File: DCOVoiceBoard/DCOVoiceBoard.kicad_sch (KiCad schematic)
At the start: 0 parts

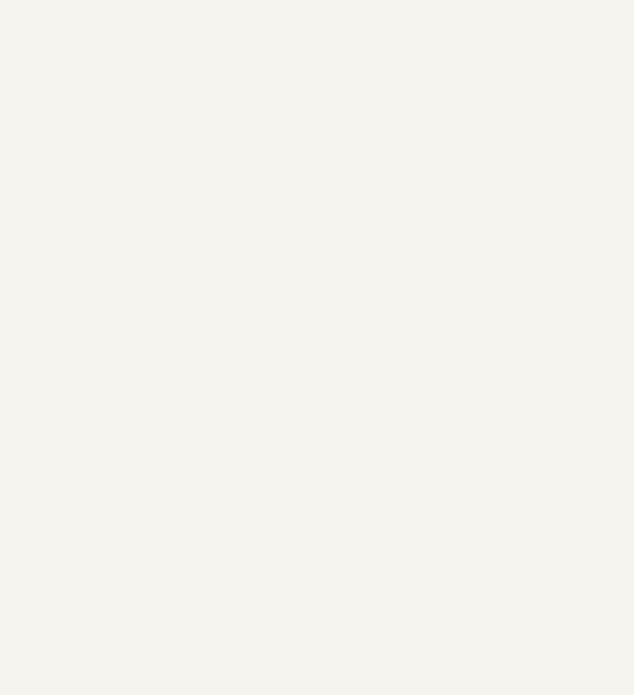
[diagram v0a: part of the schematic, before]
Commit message: voice board rough schematic
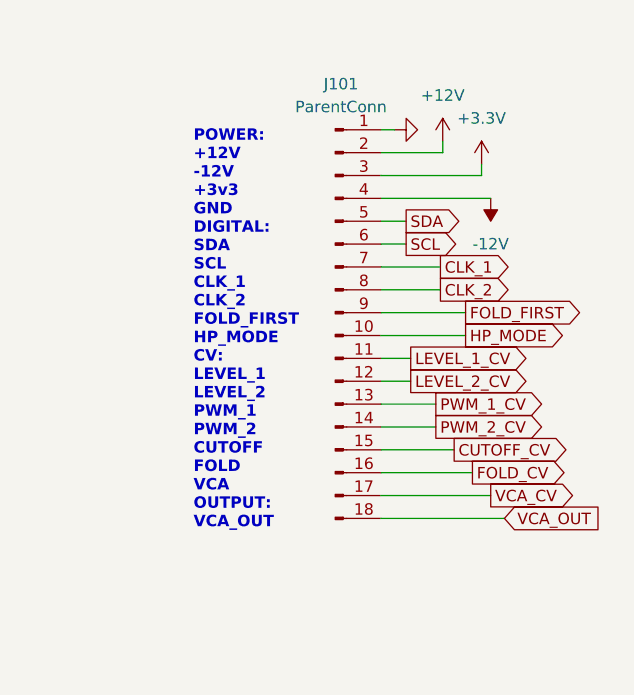
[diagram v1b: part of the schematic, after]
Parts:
- added J101: ParentConn, symbol Connector:Conn_01x18_Pin
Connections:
- new net +12V: J101.2 (Pin_2)
- new net +3.3V: J101.3 (Pin_3)
- new net -12V: J101.4 (Pin_4)
- new net CLK_1: J101.7 (Pin_7)
- new net CLK_2: J101.8 (Pin_8)
- new net CUTOFF_CV: J101.15 (Pin_15)
- new net FOLD_CV: J101.16 (Pin_16)
- new net FOLD_FIRST: J101.9 (Pin_9)
- new net GND: J101.1 (Pin_1)
- new net HP_MODE: J101.10 (Pin_10)
- new net LEVEL_1_CV: J101.11 (Pin_11)
- new net LEVEL_2_CV: J101.12 (Pin_12)
- new net PWM_1_CV: J101.13 (Pin_13)
- new net PWM_2_CV: J101.14 (Pin_14)
- new net SCL: J101.6 (Pin_6)
- new net SDA: J101.5 (Pin_5)
- new net VCA_CV: J101.17 (Pin_17)
- new net VCA_OUT: J101.18 (Pin_18)
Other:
- note added: "POWER: +12V -12V +3v3 GND DIGITAL: SDA SCL CLK_1 CLK_2 FOLD_FIRST HP_MODE CV: LEVEL_1 LEVEL_2 PWM_1 PWM_2 CUTOFF FOLD VCA OUTPUT: VCA_OUT"

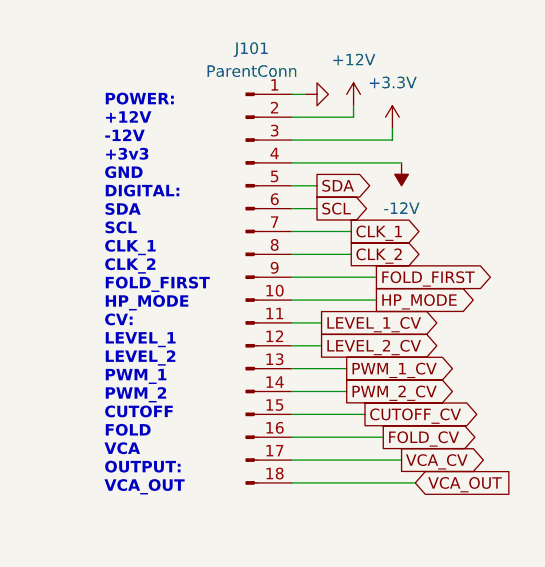
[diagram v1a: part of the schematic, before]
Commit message: net classes, osc layout
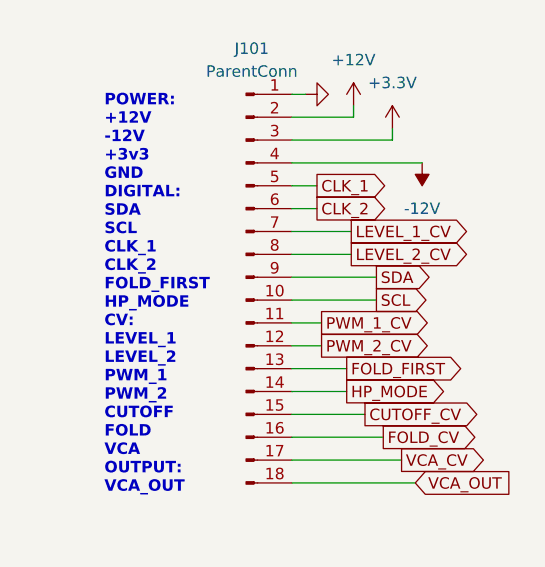
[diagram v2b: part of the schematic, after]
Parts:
- J101: footprint (none) -> Connector_PinHeader_2.54mm:PinHeader_1x18_P2.54mm_Vertical
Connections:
- net CLK_1: now also J101.5 (Pin_5); no longer J101.7 (Pin_7)
- net CLK_2: now also J101.6 (Pin_6); no longer J101.8 (Pin_8)
- net FOLD_FIRST: now also J101.13 (Pin_13); no longer J101.9 (Pin_9)
- net HP_MODE: now also J101.14 (Pin_14); no longer J101.10 (Pin_10)
- net LEVEL_1_CV: now also J101.7 (Pin_7); no longer J101.11 (Pin_11)
- net LEVEL_2_CV: now also J101.8 (Pin_8); no longer J101.12 (Pin_12)
- net PWM_1_CV: now also J101.11 (Pin_11); no longer J101.13 (Pin_13)
- net PWM_2_CV: now also J101.12 (Pin_12); no longer J101.14 (Pin_14)
- net SCL: now also J101.10 (Pin_10); no longer J101.6 (Pin_6)
- net SDA: now also J101.9 (Pin_9); no longer J101.5 (Pin_5)
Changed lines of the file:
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@@
     (stroke (width 0) (type default))
   )
-  (wire (pts (xy 119.888 43.18) (xy 132.08 43.18))
+  (wire (pts (xy 119.888 43.18) (xy 134.366 43.18))
     (stroke (width 0) (type default))
   )
@@
     (effects (font (size 1.27 1.27) bold) (justify left bottom))
   )
-  (global_label "PWM_2_CV" (shape output) (at 125.984 68.58 0) (fields_autoplaced)
-    (effects (font (size 1.27 1.27)) (justify left))
-    (property "Intersheetrefs" "${INTERSHEET_REFS}" (at 138.6453 68.58 0)
+  (global_label "PWM_2_CV" (shape output) (at 123.19 63.5 0) (fields_autoplaced)
+    (effects (font (size 1.27 1.27)) (justify left))
+    (property "Intersheetrefs" "${INTERSHEET_REFS}" (at 135.8513 63.5 0)
       (effects (font (size 1.27 1.27)) (justify left) hide)
     )
@@
     )
   )
-  (global_label "CLK_1" (shape output) (at 126.492 50.8 0) (fields_autoplaced)
-    (effects (font (size 1.27 1.27)) (justify left))
-    (property "Intersheetrefs" "${INTERSHEET_REFS}" (at 135.2224 50.8 0)
-      (effects (font (size 1.27 1.27)) (justify left) hide)
-    )
-  )
-  (global_label "SCL" (shape output) (at 122.682 48.26 0) (fields_autoplaced)
-    (effects (font (size 1.27 1.27)) (justify left))
-    (property "Intersheetrefs" "${INTERSHEET_REFS}" (at 129.1748 48.26 0)
-      (effects (font (size 1.27 1.27)) (justify left) hide)
-    )
-  )
-  (global_label "PWM_1_CV" (shape output) (at 125.984 66.04 0) (fields_autoplaced)
-    (effects (font (size 1.27 1.27)) (justify left))
-    (property "Intersheetrefs" "${INTERSHEET_REFS}" (at 138.6453 66.04 0)
+  (global_label "CLK_1" (shape output) (at 122.682 45.72 0) (fields_autoplaced)
+    (effects (font (size 1.27 1.27)) (justify left))
+    (property "Intersheetrefs" "${INTERSHEET_REFS}" (at 131.4124 45.72 0)
+      (effects (font (size 1.27 1.27)) (justify left) hide)
+    )
+  )
+  (global_label "SCL" (shape output) (at 129.286 58.42 0) (fields_autoplaced)
+    (effects (font (size 1.27 1.27)) (justify left))
+    (property "Intersheetrefs" "${INTERSHEET_REFS}" (at 135.7788 58.42 0)
+      (effects (font (size 1.27 1.27)) (justify left) hide)
+    )
+  )
+  (global_label "PWM_1_CV" (shape output) (at 123.19 60.96 0) (fields_autoplaced)
+    (effects (font (size 1.27 1.27)) (justify left))
+    (property "Intersheetrefs" "${INTERSHEET_REFS}" (at 135.8513 60.96 0)
       (effects (font (size 1.27 1.27)) (justify left) hide)
     )
@@
     )
   )
-  (global_label "LEVEL_2_CV" (shape output) (at 123.19 63.5 0) (fields_autoplaced)
-    (effects (font (size 1.27 1.27)) (justify left))
-    (property "Intersheetrefs" "${INTERSHEET_REFS}" (at 137.1213 63.5 0)
+  (global_label "LEVEL_2_CV" (shape output) (at 126.492 53.34 0) (fields_autoplaced)
+    (effects (font (size 1.27 1.27)) (justify left))
+    (property "Intersheetrefs" "${INTERSHEET_REFS}" (at 140.4233 53.34 0)
       (effects (font (size 1.27 1.27)) (justify left) hide)
     )
@@
     )
   )
-  (global_label "CLK_2" (shape output) (at 126.492 53.34 0) (fields_autoplaced)
-    (effects (font (size 1.27 1.27)) (justify left))
-    (property "Intersheetrefs" "${INTERSHEET_REFS}" (at 135.2224 53.34 0)
-      (effects (font (size 1.27 1.27)) (justify left) hide)
-    )
-  )
-  (global_label "SDA" (shape output) (at 122.682 45.72 0) (fields_autoplaced)
-    (effects (font (size 1.27 1.27)) (justify left))
-    (property "Intersheetrefs" "${INTERSHEET_REFS}" (at 129.2353 45.72 0)
-      (effects (font (size 1.27 1.27)) (justify left) hide)
-    )
-  )
-  (global_label "HP_MODE" (shape output) (at 129.286 58.42 0) (fields_autoplaced)
-    (effects (font (size 1.27 1.27)) (justify left))
-    (property "Intersheetrefs" "${INTERSHEET_REFS}" (at 141.0402 58.42 0)
-      (effects (font (size 1.27 1.27)) (justify left) hide)
-    )
-  )
-  (global_label "FOLD_FIRST" (shape output) (at 129.286 55.88 0) (fields_autoplaced)
-    (effects (font (size 1.27 1.27)) (justify left))
-    (property "Intersheetrefs" "${INTERSHEET_REFS}" (at 143.0965 55.88 0)
-      (effects (font (size 1.27 1.27)) (justify left) hide)
-    )
-  )
-  (global_label "LEVEL_1_CV" (shape output) (at 123.19 60.96 0) (fields_autoplaced)
-    (effects (font (size 1.27 1.27)) (justify left))
-    (property "Intersheetrefs" "${INTERSHEET_REFS}" (at 137.1213 60.96 0)
+  (global_label "CLK_2" (shape output) (at 122.682 48.26 0) (fields_autoplaced)
+    (effects (font (size 1.27 1.27)) (justify left))
+    (property "Intersheetrefs" "${INTERSHEET_REFS}" (at 131.4124 48.26 0)
+      (effects (font (size 1.27 1.27)) (justify left) hide)
+    )
+  )
+  (global_label "SDA" (shape output) (at 129.286 55.88 0) (fields_autoplaced)
+    (effects (font (size 1.27 1.27)) (justify left))
+    (property "Intersheetrefs" "${INTERSHEET_REFS}" (at 135.8393 55.88 0)
+      (effects (font (size 1.27 1.27)) (justify left) hide)
+    )
+  )
+  (global_label "HP_MODE" (shape output) (at 125.984 68.58 0) (fields_autoplaced)
+    (effects (font (size 1.27 1.27)) (justify left))
+    (property "Intersheetrefs" "${INTERSHEET_REFS}" (at 137.7382 68.58 0)
+      (effects (font (size 1.27 1.27)) (justify left) hide)
+    )
+  )
+  (global_label "FOLD_FIRST" (shape output) (at 125.984 66.04 0) (fields_autoplaced)
+    (effects (font (size 1.27 1.27)) (justify left))
+    (property "Intersheetrefs" "${INTERSHEET_REFS}" (at 139.7945 66.04 0)
+      (effects (font (size 1.27 1.27)) (justify left) hide)
+    )
+  )
+  (global_label "LEVEL_1_CV" (shape output) (at 126.492 50.8 0) (fields_autoplaced)
+    (effects (font (size 1.27 1.27)) (justify left))
+    (property "Intersheetrefs" "${INTERSHEET_REFS}" (at 140.4233 50.8 0)
       (effects (font (size 1.27 1.27)) (justify left) hide)
     )
@@
       (effects (font (size 1.27 1.27)))
     )
-    (property "Footprint" "" (at 114.808 55.88 0)
+    (property "Footprint" "Connector_PinHeader_2.54mm:PinHeader_1x18_P2.54mm_Vertical" (at 114.808 55.88 0)
       (effects (font (size 1.27 1.27)) hide)
     )
@@
     )
   )
-  (symbol (lib_id "power:-12V") (at 132.08 43.18 180) (unit 1)
-    (in_bom yes) (on_board yes) (dnp no) (fields_autoplaced)
-    (property "Reference" "#PWR0104" (at 132.08 45.72 0)
-      (effects (font (size 1.27 1.27)) hide)
-    )
-    (property "Value" "-12V" (at 132.08 48.26 0)
-      (effects (font (size 1.27 1.27)))
-    )
-    (property "Footprint" "" (at 132.08 43.18 0)
-      (effects (font (size 1.27 1.27)) hide)
-    )
-    (property "Datasheet" "" (at 132.08 43.18 0)
-      (effects (font (size 1.27 1.27)) hide)
-    )
+  (symbol (lib_id "power:-12V") (at 134.366 43.18 180) (unit 1)
+    (in_bom yes) (on_board yes) (dnp no) (fields_autoplaced)
+    (property "Reference" "#PWR0104" (at 134.366 45.72 0)
+      (effects (font (size 1.27 1.27)) hide)
+    )
+    (property "Value" "-12V" (at 134.366 48.26 0)
+      (effects (font (size 1.27 1.27)))
+    )
+    (property "Footprint" "" (at 134.366 43.18 0)
+      (effects (font (size 1.27 1.27)) hide)
+    )
+    (property "Datasheet" "" (at 134.366 43.18 0)
+      (effects (font (size 1.27 1.27)) hide)
+    )

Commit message: motherboard hardware
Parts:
- removed J101: ParentConn, Connector_PinHeader_2.54mm:PinHeader_1x18_P2.54mm_Vertical, symbol Connector:Conn_01x18_Pin
- added C302 (x2), C303 (x2): 100n, Capacitor_SMD:C_0805_2012Metric, symbol Device:C
- added J101: VoiceHeader, Connector_PinHeader_2.54mm:PinHeader_1x18_P2.54mm_Vertical, symbol Connector:VoiceBoardConnector_18p
- added U302 (x2): TMUX4053, Package_SO:TSSOP-16_4.4x5mm_P0.65mm, symbol Analog_Switch:TMUX4053
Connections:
- net +12V: now also C302.1, C302.1, J101.2 (+12V), U302.16 (VDD), U302.16 (VDD)
- net +3.3V: now also J101.3 (+3v3)
- net -12V: now also C303.1, C303.1, J101.4 (-12V), U302.7 (VSS), U302.7 (VSS)
- net CLK_1: now also J101.6 (CLK1)
- net CLK_2: now also J101.5 (CLK2)
- net CUTOFF_CV: now also J101.13 (CutoffCV)
- net FOLD_CV: now also J101.14 (FoldCV)
- net FOLD_FIRST: now also J101.11 (FoldFirst), U302.10 (S2), U302.11 (S1), U302.9 (S3), U302.9 (S3)
- net GND: now also C302.2, C302.2, C303.2, C303.2, J101.1 (GND), U302.2 (B0), U302.6 (INH), U302.6 (INH), U302.8 (GND), U302.8 (GND)
- net HP_MODE: now also J101.12 (HPMode), U302.10 (S2), U302.11 (S1)
- net LEVEL_1_CV: now also J101.8 (L1)
- net LEVEL_2_CV: now also J101.7 (L2)
- net PWM_1_CV: now also J101.10 (PWM1)
- net PWM_2_CV: now also J101.9 (PWM2)
- net SCL: now also J101.18 (SCL)
- net SDA: now also J101.17 (SDA)
- net VCA_CV: now also J101.15 (VCACV)
- net VCA_OUT: now also J101.16 (VoiceOut)
- new net FILTER_IN: U302.1 (B1), U302.12 (A0), U302.13 (A1), U302.4 (C)
- new net FILTER_OUT: U302.2 (B0), U302.4 (C)
- new net FOLDER_IN: U302.15 (B), U302.5 (C0)
- new net FOLDER_OUT: U302.14 (A), U302.3 (C1)
- new net HP_IN: U302.15 (B)
- new net LP_IN: U302.14 (A)
- new net OSC_MIX: U302.1 (B1), U302.5 (C0)
- new net VCA_IN: U302.12 (A0), U302.3 (C1)
- no-connect marks 0 -> 1
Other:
- note added: "Logic high on 'FOLD_FIRST' = route to the VCA, otherwise to the wave folder"
- note added: "Logic high on HP_MODE = high pass mode"
- note added: "Motherboard Header"
- note added: "Signal Multiplexers"
- note removed: "POWER: +12V -12V +3v3 GND DIGITAL: SDA SCL CLK_1 CLK_2 FOLD_FIRST HP_MODE CV: LEVEL_1 LEVEL_2 PWM_1 PWM_2 CUTOFF FOLD VCA OUTPUT: VCA_OUT"
